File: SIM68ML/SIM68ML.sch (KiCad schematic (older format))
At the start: 26 parts, among them IC1 SIM68M, J1 Conn_01x05, J2 Conn_01x05, U2 AP7365-W-7

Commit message: Part Numbers Added
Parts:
- AE1: Part (none) -> C88374
- BT1: Part (none) -> C238097
- C1: Part (none) -> C87998
- C2, C6: Part (none) -> C42998
- C3, C4: Part (none) -> C396719
- IC1: Description GPS Receiver -> (none); Height 2 -> (none); Manufacturer_Name SIMCOM -> (none); Manufacturer_Part_Number SIM28M -> (none); Part (none) -> OTTO
- L1: Part (none) -> C142204
- R1, R2: Part (none) -> C245184
- R3: Part (none) -> C99198
- R4: Part (none) -> C269698
- R5: Part (none) -> C176153
- R7: Part (none) -> C163436
- R8: Part (none) -> C103426
- U2: Part (none) -> C264087
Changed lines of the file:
@@
 F 2 "Package_TO_SOT_SMD:SOT-23-5" H 2450 1625 50  0001 C CNN
 F 3 "https://www.diodes.com/assets/Datasheets/AP2127.pdf" H 2450 1400 50  0001 C CNN
+F 4 "C264087" H 2450 1300 50  0001 C CNN "Part"
 	1    2450 1300
 	1    0    0    -1
@@
 F 2 "Resistor_SMD:R_0603_1608Metric" V 3040 1190 50  0001 C CNN
 F 3 "~" H 3000 1200 50  0001 C CNN
+F 4 "C163436" V 3000 1200 50  0001 C CNN "Part"
 	1    3000 1200
 	0    -1   -1   0
@@
 F 2 "Resistor_SMD:R_0603_1608Metric" V 3240 1490 50  0001 C CNN
 F 3 "~" H 3200 1500 50  0001 C CNN
+F 4 "C103426" H 3200 1500 50  0001 C CNN "Part"
 	1    3200 1500
 	-1   0    0    1
@@
 F 2 "Resistor_SMD:R_0603_1608Metric" V 2190 2690 50  0001 C CNN
 F 3 "~" H 2150 2700 50  0001 C CNN
+F 4 "C245184" V 2150 2700 50  0001 C CNN "Part"
 	1    2150 2700
 	0    -1   1    0
@@
 F 2 "Resistor_SMD:R_0603_1608Metric" V 5040 3190 50  0001 C CNN
 F 3 "~" H 5000 3200 50  0001 C CNN
+F 4 "C269698" V 5000 3200 50  0001 C CNN "Part"
 	1    5000 3200
 	0    -1   1    0
@@
 F 2 "Resistor_SMD:R_0603_1608Metric" V 5040 2890 50  0001 C CNN
 F 3 "~" H 5000 2900 50  0001 C CNN
+F 4 "C176153" V 5000 2900 50  0001 C CNN "Part"
 	1    5000 2900
 	0    -1   1    0
@@
 F 2 "Resistor_SMD:R_0603_1608Metric" V 2190 2590 50  0001 C CNN
 F 3 "~" H 2150 2600 50  0001 C CNN
+F 4 "C245184" V 2150 2600 50  0001 C CNN "Part"
 	1    2150 2600
 	0    -1   -1   0
@@
 F 2 "Battery:BatteryHolder_Keystone_3000_1x12mm" V 2550 3660 50  0001 C CNN
 F 3 "~" V 2550 3660 50  0001 C CNN
+F 4 "C238097" H 2550 3600 50  0001 C CNN "Part"
 	1    2550 3600
 	-1   0    0    -1
@@
 F 2 "Capacitor_SMD:C_0805_2012Metric" H 1388 3300 50  0001 C CNN
 F 3 "~" H 1350 3450 50  0001 C CNN
+F 4 "C87998" H 1350 3450 50  0001 C CNN "Part"
 	1    1350 3450
 	1    0    0    -1
@@
 F 2 "Capacitor_SMD:C_0603_1608Metric" H 1738 3300 50  0001 C CNN
 F 3 "~" H 1700 3450 50  0001 C CNN
+F 4 "C42998" H 1700 3450 50  0001 C CNN "Part"
 	1    1700 3450
 	1    0    0    -1
@@
 F 2 "Inductor_SMD:L_0603_1608Metric" H 5400 2900 50  0001 C CNN
 F 3 "~" H 5400 2900 50  0001 C CNN
+F 4 "C142204" V 5400 2900 50  0001 C CNN "Part"
 	1    5400 2900
 	0    1    -1   0
@@
 F 2 "Capacitor_SMD:C_0603_1608Metric" H 4738 2450 50  0001 C CNN
 F 3 "~" H 4700 2600 50  0001 C CNN
+F 4 "C42998" H 4700 2600 50  0001 C CNN "Part"
 	1    4700 2600
 	1    0    0    -1
@@
 F 2 "Connector_Coaxial:U.FL_Hirose_U.FL-R-SMT-1_Vertical" H 6350 2800 50  0001 C CNN
 F 3 "~" H 6350 2800 50  0001 C CNN
+F 4 "C88374" H 6350 2700 50  0001 C CNN "Part"
 	1    6350 2700
 	1    0    0    -1
@@
 F 2 "Capacitor_SMD:C_0805_2012Metric" H 1588 1350 50  0001 C CNN
 F 3 "~" H 1550 1500 50  0001 C CNN
+F 4 "C396719" H 1550 1500 50  0001 C CNN "Part"
 	1    1550 1500
 	1    0    0    -1
@@
 F 2 "Resistor_SMD:R_0603_1608Metric" V 1890 1290 50  0001 C CNN
 F 3 "~" H 1850 1300 50  0001 C CNN
+F 4 "C99198" V 1850 1300 50  0001 C CNN "Part"
 	1    1850 1300
 	0    -1   1    0
@@
 F 2 "Capacitor_SMD:C_0805_2012Metric" H 3488 1350 50  0001 C CNN
 F 3 "~" H 3450 1500 50  0001 C CNN
+F 4 "C396719" H 3450 1500 50  0001 C CNN "Part"
 	1    3450 1500
 	1    0    0    -1
@@
 F 2 "SIM28M" H 4050 2600 50  0001 L CNN
 F 3 "http://simcomm2m.com/UploadFile/TechnicalFile/SIM28M_Hardware%20Design_V1.00.pdf" H 4050 1700 50  0001 L CNN
-F 4 "GPS Receiver" H 4050 1800 50  0001 L CNN "Description"
-F 5 "2" H 4050 2300 50  0001 L CNN "Height"
-F 6 "SIMCOM" H 4050 2000 50  0001 L CNN "Manufacturer_Name"
-F 7 "SIM28M" H 4050 2100 50  0001 L CNN "Manufacturer_Part_Number"
+F 4 "OTTO" H 2700 2500 50  0001 C CNN "Part"
 	1    2700 2500
 	1    0    0    -1

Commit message: Power LED added
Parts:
- removed R7: 68K, Resistor_SMD:R_0603_1608Metric, symbol Device:R_US
- removed R8: 22K, Resistor_SMD:R_0603_1608Metric, symbol Device:R_US
- removed U2: AP7365-W-7, Package_TO_SOT_SMD:SOT-23-5, symbol Regulator_Linear:AP2127K-ADJ
- added D1: LED, LED_SMD:LED_0603_1608Metric, symbol Device:LED
- added JP2: SolderJumper_2_Bridged, Jumper:SolderJumper-2_P1.3mm_Bridged_RoundedPad1.0x1.5mm, symbol Jumper:SolderJumper_2_Bridged
- added R6: 680E, Resistor_SMD:R_0603_1608Metric, symbol Device:R_US
- added U1: AP2127K-3.3, Package_TO_SOT_SMD:SOT-23-5, symbol Regulator_Linear:AP2127K-3.3
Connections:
- wire segments 87 -> 84
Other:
- moved on the sheet: C3, C4, R3
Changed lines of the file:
@@
 Comment4 ""
 $EndDescr
-Text GLabel 3600 1050 2    50   Input ~ 0
+Text GLabel 3125 950  2    50   Input ~ 0
 3V3
 Wire Wire Line
-	1550 1350 1550 1300
-Wire Wire Line
-	1550 1650 1550 1800
+	1150 1325 1150 1200
+Wire Wire Line
+	1150 1625 1150 1925
 $Comp
 L power:GND #PWR0103
 U 1 1 5DFA7870
-P 2450 1900
-F 0 "#PWR0103" H 2450 1650 50  0001 C CNN
-F 1 "GND" H 2455 1727 50  0000 C CNN
-F 2 "" H 2450 1900 50  0001 C CNN
-F 3 "" H 2450 1900 50  0001 C CNN
-	1    2450 1900
-	1    0    0    -1
-$EndComp
-$Comp
-L Regulator_Linear:AP2127K-ADJ U2
-U 1 1 5E2BA0AD
-P 2450 1300
-F 0 "U2" H 2450 1640 50  0000 C CNN
-F 1 "AP7365-W-7" H 2450 1550 50  0000 C CNN
-F 2 "Package_TO_SOT_SMD:SOT-23-5" H 2450 1625 50  0001 C CNN
-F 3 "https://www.diodes.com/assets/Datasheets/AP2127.pdf" H 2450 1400 50  0001 C CNN
-F 4 "C264087" H 2450 1300 50  0001 C CNN "Part"
-	1    2450 1300
-	1    0    0    -1
-$EndComp
-$Comp
-L Device:R_US R7
-U 1 1 5E34715F
-P 3000 1200
-F 0 "R7" V 3068 1246 50  0000 L CNN
-F 1 "68K" V 3068 1155 50  0000 R CNN
-F 2 "Resistor_SMD:R_0603_1608Metric" V 3040 1190 50  0001 C CNN
-F 3 "~" H 3000 1200 50  0001 C CNN
-F 4 "C163436" V 3000 1200 50  0001 C CNN "Part"
-	1    3000 1200
-	0    -1   -1   0
-$EndComp
-$Comp
-L Device:R_US R8
-U 1 1 5E35753D
-P 3200 1500
-F 0 "R8" H 3300 1450 50  0000 L CNN
-F 1 "22K" H 3400 1550 50  0000 R CNN
-F 2 "Resistor_SMD:R_0603_1608Metric" V 3240 1490 50  0001 C CNN
-F 3 "~" H 3200 1500 50  0001 C CNN
-F 4 "C103426" H 3200 1500 50  0001 C CNN "Part"
-	1    3200 1500
-	-1   0    0    1
-$EndComp
-Wire Wire Line
-	3200 1300 2750 1300
-Wire Wire Line
-	3150 1200 3200 1200
-Wire Wire Line
-	3200 1350 3200 1300
+P 2050 2000
+F 0 "#PWR0103" H 2050 1750 50  0001 C CNN
+F 1 "GND" H 2055 1827 50  0000 C CNN
+F 2 "" H 2050 2000 50  0001 C CNN
+F 3 "" H 2050 2000 50  0001 C CNN
+	1    2050 2000
+	1    0    0    -1
+$EndComp
 $Comp
 L Device:R_US R1
@@
 Connection ~ 1350 3200
 Wire Wire Line
-	1550 1800 2450 1800
-Wire Wire Line
-	3200 1650 3200 1800
-Wire Wire Line
-	3200 1300 3200 1200
-Connection ~ 3200 1300
-Wire Wire Line
-	2750 1200 2800 1200
-Wire Wire Line
-	2800 1200 2800 1050
-Connection ~ 2800 1200
-Wire Wire Line
-	2800 1200 2850 1200
-Wire Wire Line
-	2800 1050 3450 1050
+	1150 1925 2050 1925
 $Comp
 L Device:C C3
 U 1 1 5DCB3070
-P 1550 1500
-F 0 "C3" H 1665 1545 50  0000 L CNN
-F 1 "1uF" H 1665 1455 50  0000 L CNN
-F 2 "Capacitor_SMD:C_0805_2012Metric" H 1588 1350 50  0001 C CNN
-F 3 "~" H 1550 1500 50  0001 C CNN
-F 4 "C396719" H 1550 1500 50  0001 C CNN "Part"
-	1    1550 1500
-	1    0    0    -1
-$EndComp
-Wire Wire Line
-	3450 1350 3450 1050
-Connection ~ 3450 1050
-Wire Wire Line
-	3450 1050 3600 1050
-Wire Wire Line
-	3450 1650 3450 1800
-Wire Wire Line
-	3450 1800 3200 1800
-Connection ~ 3200 1800
-Text GLabel 1300 1200 0    50   Input ~ 0
+P 1150 1475
+F 0 "C3" H 1265 1520 50  0000 L CNN
+F 1 "1uF" H 1265 1430 50  0000 L CNN
+F 2 "Capacitor_SMD:C_0805_2012Metric" H 1188 1325 50  0001 C CNN
+F 3 "~" H 1150 1475 50  0001 C CNN
+F 4 "C396719" H 1150 1475 50  0001 C CNN "Part"
+	1    1150 1475
+	1    0    0    -1
+$EndComp
+Wire Wire Line
+	2650 1250 2650 950
+Connection ~ 2650 950
+Text GLabel 900  950  0    50   Input ~ 0
 VIN
 Wire Wire Line
-	1300 1200 1550 1200
-Connection ~ 1550 1200
+	900  950  1150 950
+Connection ~ 1150 950
 Text GLabel 4600 1950 0    50   Input ~ 0
 3V3
@@
 VIN
 Wire Wire Line
-	1550 1200 2150 1200
+	1150 950  1750 950
 $Comp
 L Device:R_US R3
 U 1 1 5DCC87E2
-P 1850 1300
-F 0 "R3" V 1918 1346 50  0000 L CNN
-F 1 "10K" V 1918 1255 50  0000 R CNN
-F 2 "Resistor_SMD:R_0603_1608Metric" V 1890 1290 50  0001 C CNN
-F 3 "~" H 1850 1300 50  0001 C CNN
-F 4 "C99198" V 1850 1300 50  0001 C CNN "Part"
-	1    1850 1300
+P 1450 1200
+F 0 "R3" V 1550 1250 50  0000 L CNN
+F 1 "10K" V 1550 1150 50  0000 R CNN
+F 2 "Resistor_SMD:R_0603_1608Metric" V 1490 1190 50  0001 C CNN
+F 3 "~" H 1450 1200 50  0001 C CNN
+F 4 "C99198" V 1450 1200 50  0001 C CNN "Part"
+	1    1450 1200
 	0    -1   1    0
 $EndComp
 Wire Wire Line
-	2000 1300 2100 1300
-Wire Wire Line
-	1700 1300 1550 1300
-Connection ~ 1550 1300
-Wire Wire Line
-	1550 1300 1550 1200
-Text GLabel 2050 1500 0    50   Input ~ 0
+	1600 1200 1700 1200
+Wire Wire Line
+	1300 1200 1150 1200
+Text GLabel 1650 1400 0    50   Input ~ 0
 EN
 Wire Wire Line
-	2050 1500 2100 1500
-Wire Wire Line
-	2100 1500 2100 1300
-Connection ~ 2100 1300
-Wire Wire Line
-	2100 1300 2150 1300
+	1650 1400 1700 1400
+Wire Wire Line
+	1700 1400 1700 1200
+Wire Wire Line
+	1700 1050 1750 1050
 $Comp
 L Device:C C4
 U 1 1 5DB8E885
-P 3450 1500
-F 0 "C4" H 3565 1545 50  0000 L CNN
-F 1 "1uF" H 3565 1455 50  0000 L CNN
-F 2 "Capacitor_SMD:C_0805_2012Metric" H 3488 1350 50  0001 C CNN
-F 3 "~" H 3450 1500 50  0001 C CNN
-F 4 "C396719" H 3450 1500 50  0001 C CNN "Part"
-	1    3450 1500
+P 2650 1400
+F 0 "C4" H 2765 1445 50  0000 L CNN
+F 1 "1uF" H 2765 1355 50  0000 L CNN
+F 2 "Capacitor_SMD:C_0805_2012Metric" H 2688 1250 50  0001 C CNN
+F 3 "~" H 2650 1400 50  0001 C CNN
+F 4 "C396719" H 2650 1400 50  0001 C CNN "Part"
+	1    2650 1400
 	1    0    0    -1
 $EndComp
@@
 	1    0    0    -1
 $EndComp
-Wire Wire Line
-	2450 1600 2450 1800
-Connection ~ 2450 1800
-Wire Wire Line
-	2450 1800 3200 1800
-Wire Wire Line
-	2450 1800 2450 1900
 $Comp
 L Connector_Generic:Conn_01x05 J1
@@
 	6450 3750 5300 3750
 Connection ~ 5300 3750
+$Comp
+L Regulator_Linear:AP2127K-3.3 U1
+U 1 1 5DEF9F5A
+P 2050 1050
+F 0 "U1" H 2050 1390 50  0000 C CNN
+F 1 "AP2127K-3.3" H 2050 1300 50  0000 C CNN
+F 2 "Package_TO_SOT_SMD:SOT-23-5" H 2050 1375 50  0001 C CNN
+F 3 "https://www.diodes.com/assets/Datasheets/AP2127.pdf" H 2050 1150 50  0001 C CNN
+	1    2050 1050
+	1    0    0    -1
+$EndComp
+Wire Wire Line
+	2050 1925 2650 1925
+Wire Wire Line
+	2350 950  2650 950
+$Comp
+L Device:R_US R6
+U 1 1 5DF1FCDE
+P 3000 1425
+F 0 "R6" H 3075 1400 50  0000 L CNN
+F 1 "680E" H 3075 1475 50  0000 L CNN
+F 2 "Resistor_SMD:R_0603_1608Metric" V 3040 1415 50  0001 C CNN
+F 3 "~" H 3000 1425 50  0001 C CNN
+F 4 "C269441" V 3000 1425 50  0001 C CNN "Part"
+	1    3000 1425
+	1    0    0    1
+$EndComp
+$Comp
+L Device:LED D1
+U 1 1 5DF220F7
+P 3000 1750
+F 0 "D1" V 3038 1632 50  0000 R CNN
+F 1 "LED" V 2948 1632 50  0000 R CNN
+F 2 "LED_SMD:LED_0603_1608Metric" H 3000 1750 50  0001 C CNN
+F 3 "~" H 3000 1750 50  0001 C CNN
+F 4 "C193191" V 3000 1750 50  0001 C CNN "Part"
+	1    3000 1750
+	0    -1   -1   0
+$EndComp
+Wire Wire Line
+	3000 1575 3000 1600
+Wire Wire Line
+	3000 1900 3000 1925
+Wire Wire Line
+	3000 1925 2650 1925
+$Comp
+L Jumper:SolderJumper_2_Bridged JP2
+U 1 1 5DF32687
+P 3000 1125
+F 0 "JP2" V 3000 1192 50  0000 L CNN
+F 1 "SolderJumper_2_Bridged" V 3045 1193 50  0001 L CNN
+F 2 "Jumper:SolderJumper-2_P1.3mm_Bridged_RoundedPad1.0x1.5mm" H 3000 1125 50  0001 C CNN
+F 3 "~" H 3000 1125 50  0001 C CNN
+	1    3000 1125
+	0    1    1    0
+$EndComp
+Connection ~ 2050 1925
+Wire Wire Line
+	2050 1925 2050 2000
+Connection ~ 2650 1925
+Wire Wire Line
+	2650 1550 2650 1925
+Wire Wire Line
+	2050 1350 2050 1925
+Connection ~ 1150 1200
+Connection ~ 1700 1200
+Wire Wire Line
+	1700 1200 1700 1050
+Wire Wire Line
+	1150 950  1150 1200
+Wire Wire Line
+	2650 950  3000 950
+Wire Wire Line
+	3000 975  3000 950
+Connection ~ 3000 950
+Wire Wire Line
+	3000 950  3125 950
 $EndSCHEMATC

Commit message: Schematic PDF and 3D Renders added
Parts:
- IC1: symbol SIM28M:SIM68M -> SIM68ML-rescue:SIM68M-SIM28M
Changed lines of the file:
@@
 	4450 3100 4450 3300
 $Comp
-L SIM28M:SIM68M IC1
+L SIM68ML-rescue:SIM68M-SIM28M IC1
 U 1 1 5DBF66F0
 P 2700 2500

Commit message: Board Sizes Updated
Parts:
- H1, H2, H3, H4: footprint MountingHole:MountingHole_2.7mm_M2.5_ISO14580_Pad -> SirBoardLibrary:MountingHole_M2.5_SirBoard
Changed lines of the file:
@@
 F 0 "H1" H 5750 1050 50  0000 L CNN
 F 1 "MountingHole" H 5750 1005 50  0001 L CNN
-F 2 "MountingHole:MountingHole_2.7mm_M2.5_ISO14580_Pad" H 5650 1050 50  0001 C CNN
+F 2 "SirBoardLibrary:MountingHole_M2.5_SirBoard" H 5650 1050 50  0001 C CNN
 F 3 "~" H 5650 1050 50  0001 C CNN
 	1    5650 1050
@@
 F 0 "H2" H 5750 1700 50  0000 L CNN
 F 1 "MountingHole" H 5750 1655 50  0001 L CNN
-F 2 "MountingHole:MountingHole_2.7mm_M2.5_ISO14580_Pad" H 5650 1700 50  0001 C CNN
+F 2 "SirBoardLibrary:MountingHole_M2.5_SirBoard" H 5650 1700 50  0001 C CNN
 F 3 "~" H 5650 1700 50  0001 C CNN
 	1    5650 1700
@@
 F 0 "H3" H 6450 1700 50  0000 L CNN
 F 1 "MountingHole" H 6450 1655 50  0001 L CNN
-F 2 "MountingHole:MountingHole_2.7mm_M2.5_ISO14580_Pad" H 6350 1700 50  0001 C CNN
+F 2 "SirBoardLibrary:MountingHole_M2.5_SirBoard" H 6350 1700 50  0001 C CNN
 F 3 "~" H 6350 1700 50  0001 C CNN
 	1    6350 1700
@@
 F 0 "H4" H 6450 1050 50  0000 L CNN
 F 1 "MountingHole" H 6450 1005 50  0001 L CNN
-F 2 "MountingHole:MountingHole_2.7mm_M2.5_ISO14580_Pad" H 6350 1050 50  0001 C CNN
+F 2 "SirBoardLibrary:MountingHole_M2.5_SirBoard" H 6350 1050 50  0001 C CNN
 F 3 "~" H 6350 1050 50  0001 C CNN
 	1    6350 1050

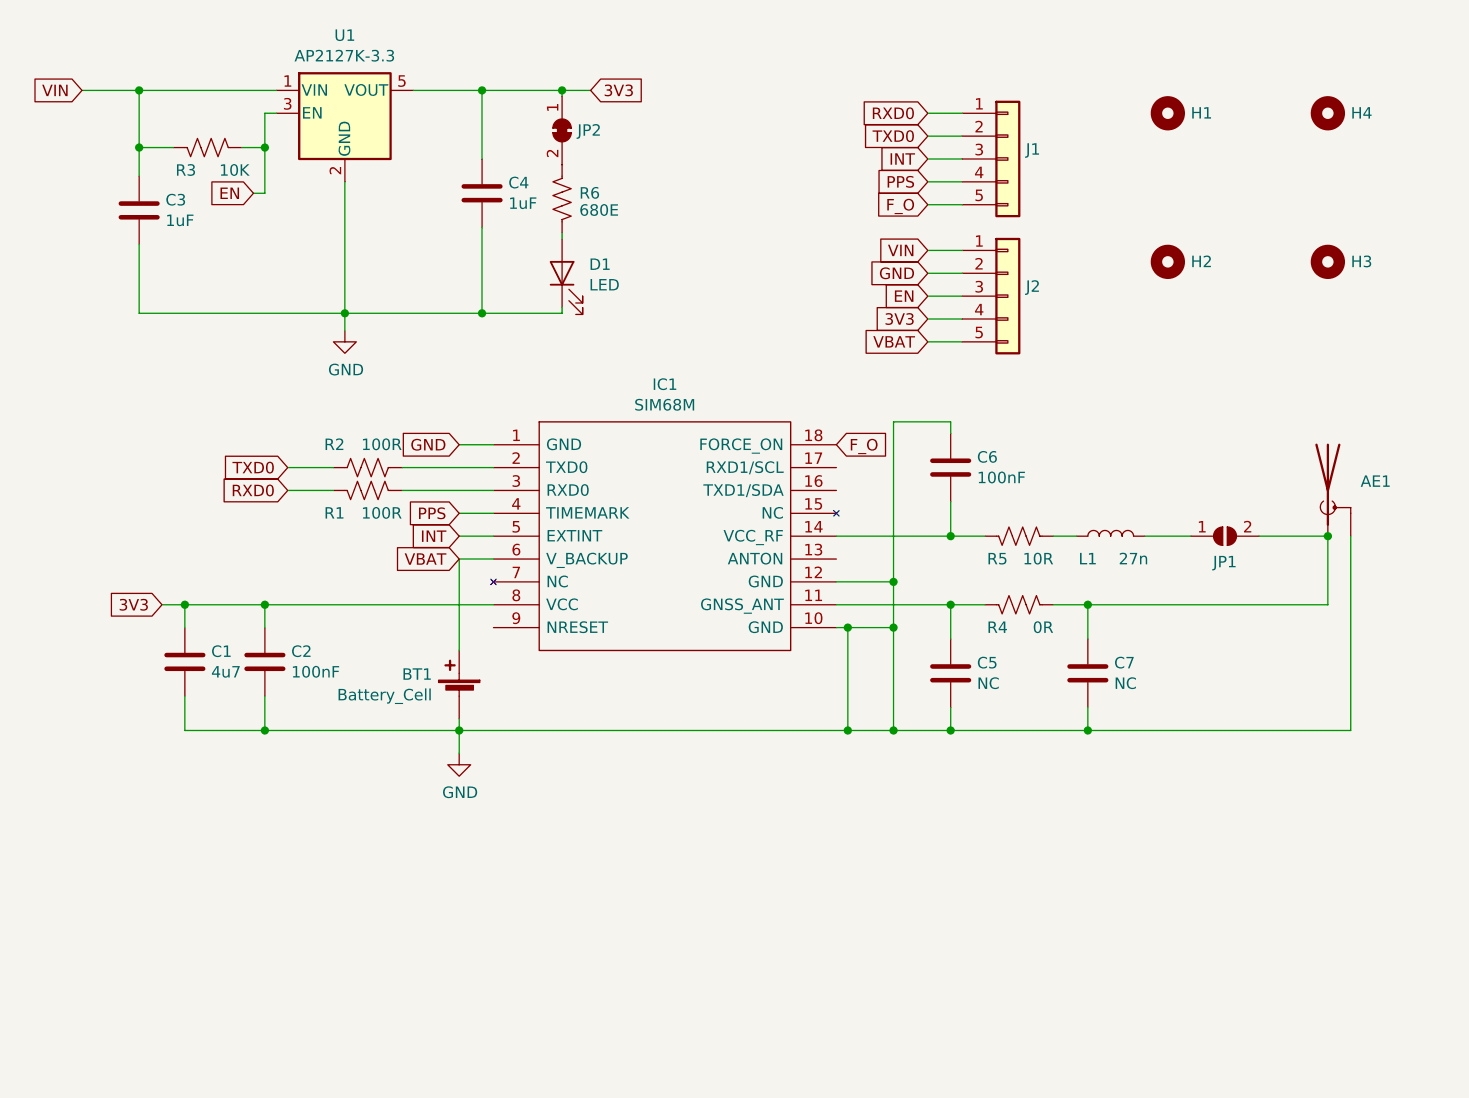
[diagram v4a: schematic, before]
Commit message: SIM68ML Revision 2
Active Antenna components removed, Battery connector changed
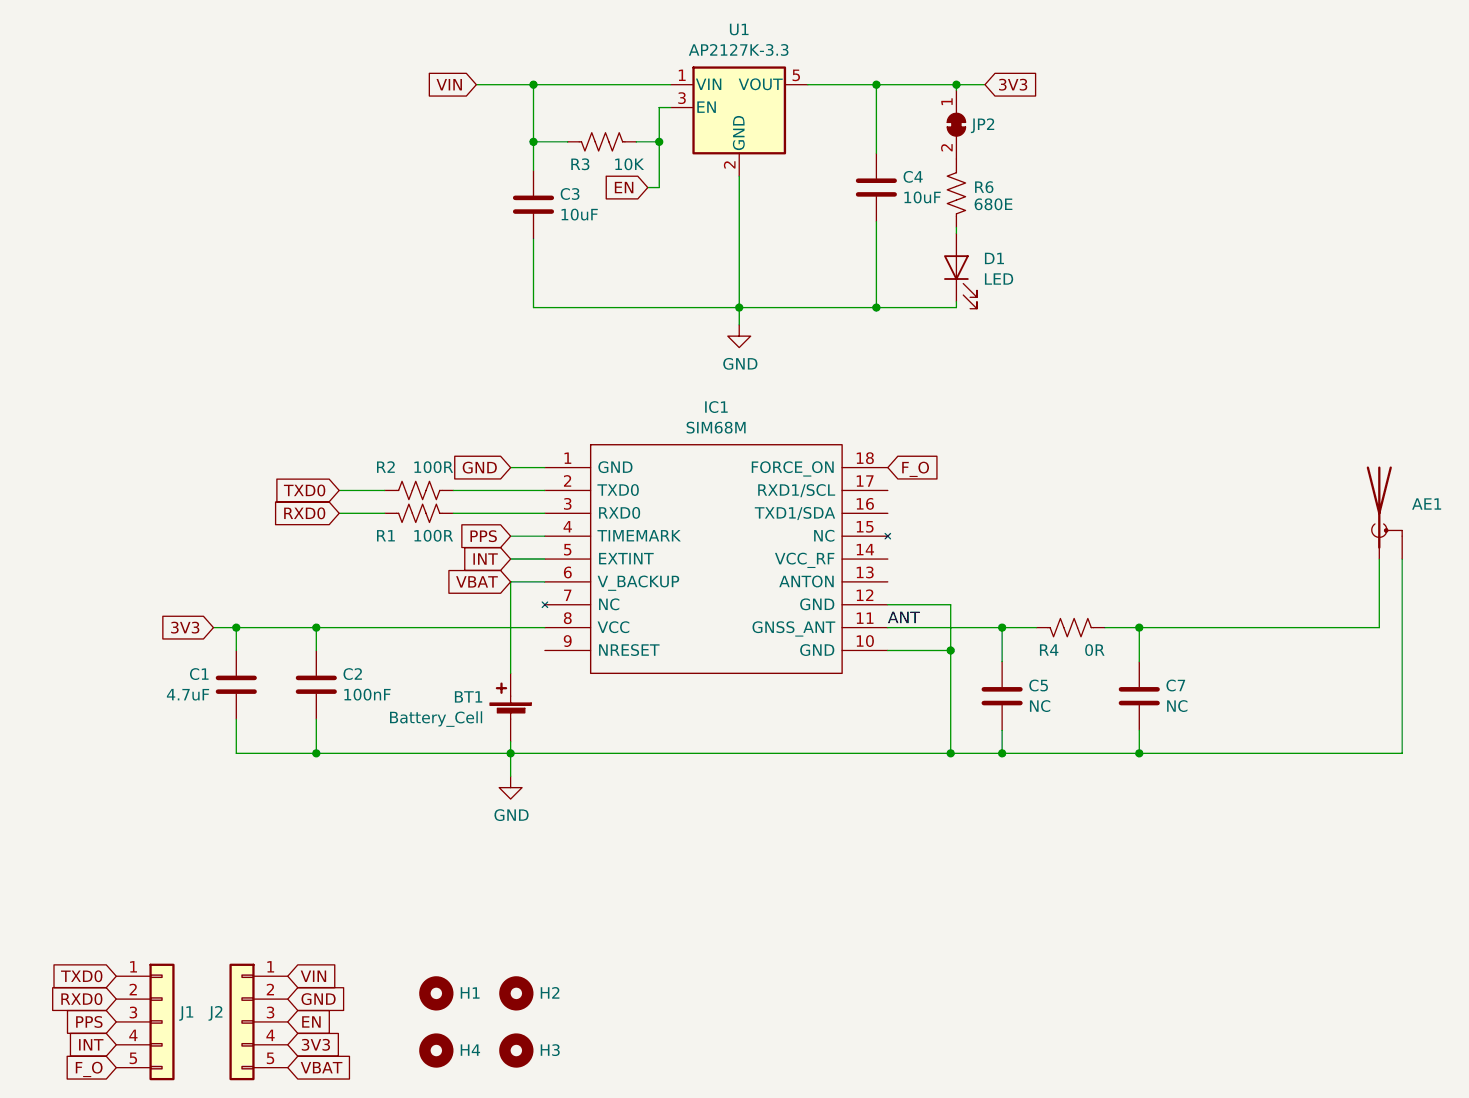
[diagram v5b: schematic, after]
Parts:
- removed C6: 100nF, Capacitor_SMD:C_0603_1608Metric, symbol Device:C
- removed JP1: SolderJumper_2_Open, Jumper:SolderJumper-2_P1.3mm_Open_RoundedPad1.0x1.5mm, symbol Jumper:SolderJumper_2_Open
- removed L1: 27n, Inductor_SMD:L_0603_1608Metric, symbol Device:L
- removed R5: 10R, Resistor_SMD:R_0603_1608Metric, symbol Device:R_US
- BT1: footprint Battery:BatteryHolder_Keystone_3000_1x12mm -> SirBoardLibrary:S8411-45R_1; Part C238097 -> C70381
- C1: value 4u7 -> 4.7uF; footprint Capacitor_SMD:C_0805_2012Metric -> Capacitor_SMD:C_0603_1608Metric; Part C87998 -> (none)
- C3, C4: value 1uF -> 10uF; Part C396719 -> C95841
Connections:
- net INT: now also J1.4 (Pin_4); no longer J1.3 (Pin_3)
- net PPS: now also J1.3 (Pin_3); no longer J1.4 (Pin_4)
- net RXD0: now also J1.2 (Pin_2); no longer J1.1 (Pin_1)
- net TXD0: now also J1.1 (Pin_1); no longer J1.2 (Pin_2)
- net ANT: now reaches C5.1, IC1.11 (GNSS_ANT), R4.1
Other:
- moved on the sheet: AE1, BT1, C1, C2, C3, C4, C5, C7, D1, H1, H2, H3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
